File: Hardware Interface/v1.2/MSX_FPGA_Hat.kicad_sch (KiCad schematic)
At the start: 24 parts, among them J1 J1, J2 J2, J3a1 J3a, J3b1 J3b, J4a1 J4a, J4b1 J4b, U1 74LVC245A, U2 74LVC245A, U3 74LVC245A, U4 74LVC245A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

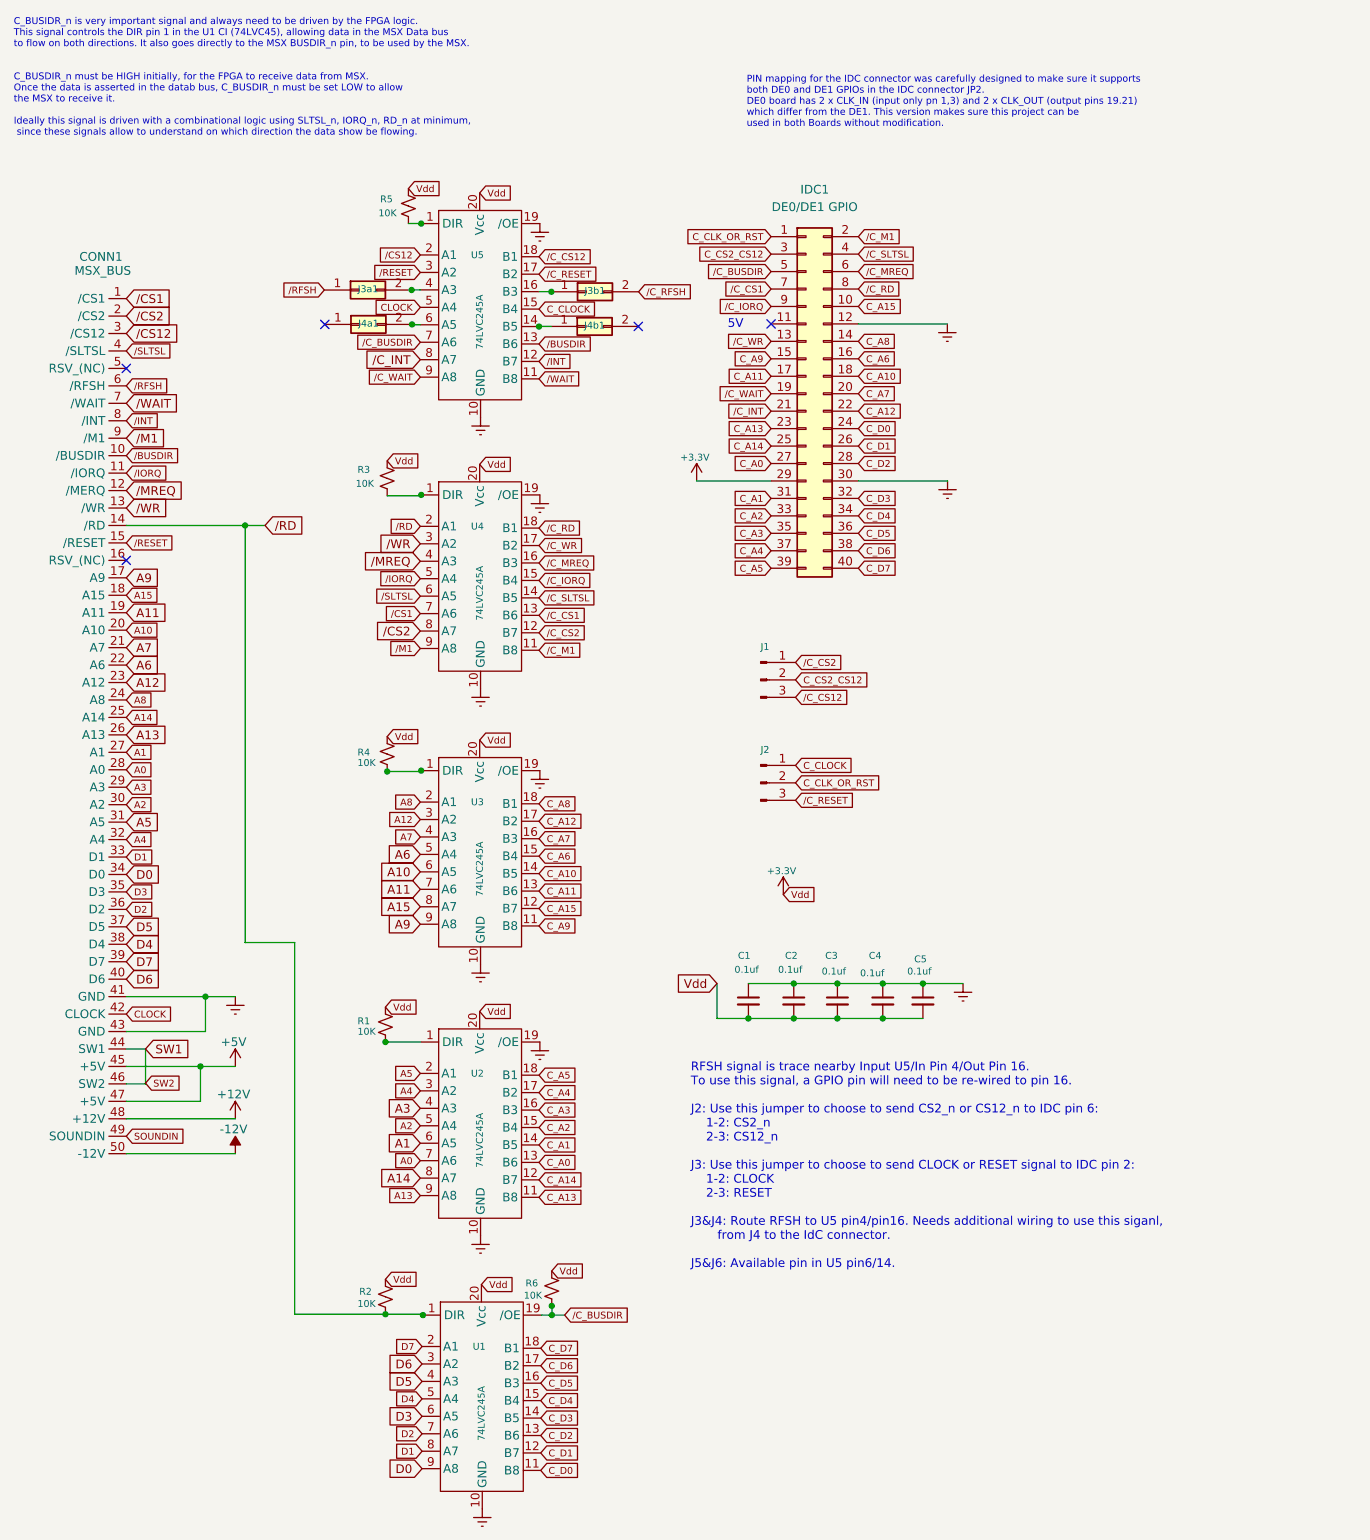
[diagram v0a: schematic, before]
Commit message: Reverted the interface schema to v1.1, as it's verified that U1 does not need to be driven by its own 7 separate pin.  BUSDIR in the FPGA will continue driving both MSX BUSDIR and U1 DIR pin
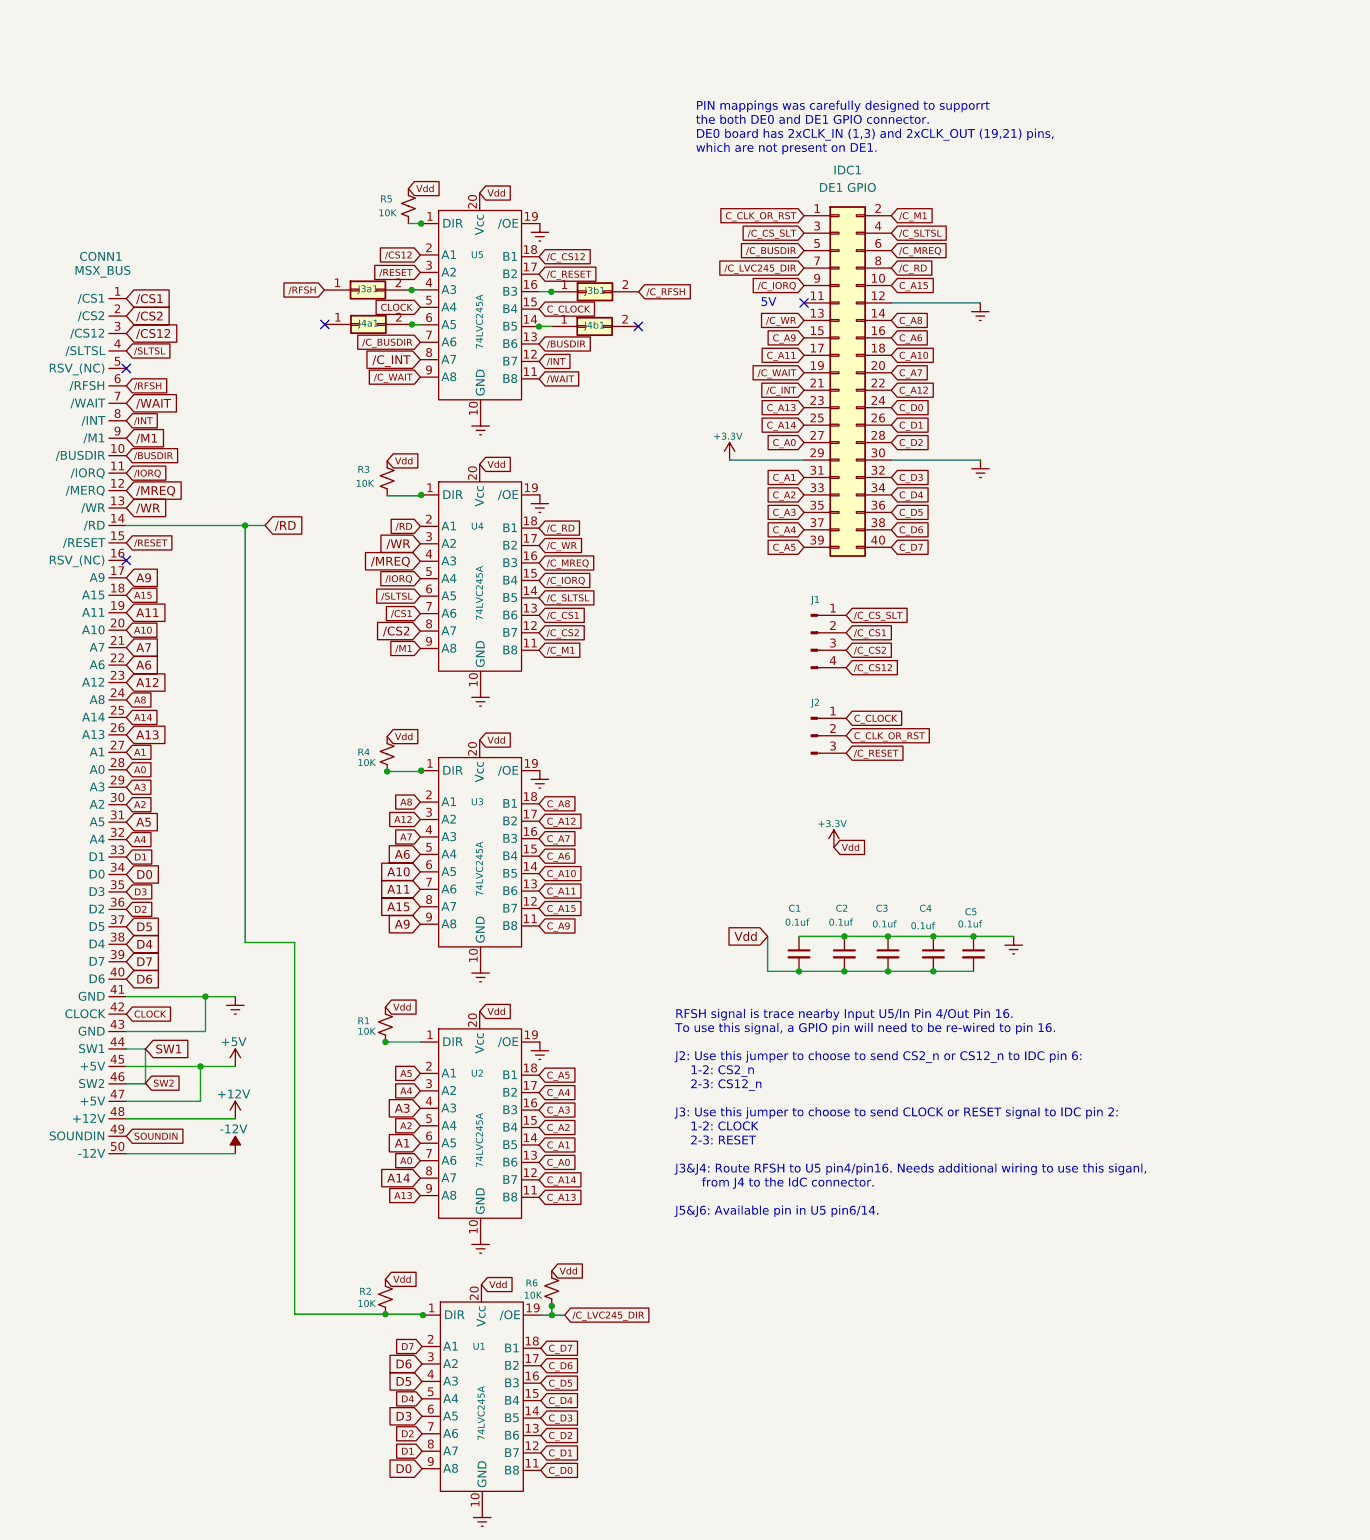
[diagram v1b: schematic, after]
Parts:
- IDC1: value DE0/DE1 GPIO -> DE1 GPIO
- J1: footprint Connector_PinHeader_2.54mm:PinHeader_1x03_P2.54mm_Vertical -> Connector_PinHeader_2.54mm:PinHeader_2x02_P2.54mm_Vertical; symbol Connector:Conn_01x03_Male -> Connector:Conn_01x04_Male
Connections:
- net /C_BUSDIR: no longer R6.2, U1.19 (/OE)
- net /C_CS1: now also J1.2 (Pin_2); no longer IDC1.7 (Pin_7)
- net /C_CS12: now also J1.4 (Pin_4); no longer J1.3 (Pin_3)
- net /C_CS2: now also J1.3 (Pin_3); no longer J1.1 (Pin_1)
- net C_CS2_CS12 renamed /C_CS_SLT
- net /C_CS_SLT: now also J1.1 (Pin_1); no longer J1.2 (Pin_2)
- new net /C_LVC245_DIR: IDC1.7 (Pin_7), R6.2, U1.19 (/OE)
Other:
- note added: "PIN mappings was carefully designed to supporrt the both DE0 and DE1 GPIO connector. DE0 board has 2xCLK_IN (1,3) and 2xCLK_OUT (19,21) pins, which are not present on DE1."
- note removed: "C_BUSIDR_n is very important signal and always need to be driven by the FPGA logic. This signal controls the DIR pin 1 in the U1 CI (74LVC45), allowing data in the MSX Data bus to flow on both directions. It also goes directly to the MSX BUSDIR_n pin, to be used by the MSX. C_BUSDIR_n must be HIGH initially, for the FPGA to receive data from MSX. Once the data is asserted in the datab bus, C_BUSD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"
- note removed: "PIN mapping for the IDC connector was carefully designed to make sure it supports both DE0 and DE1 GPIOs in the IDC connector JP2. DE0 board has 2 x CLK_IN (input only pn 1,3) and 2 x CLK_OUT (output pins 19.21) which differ from the DE1. This version makes sure this project can be used in both Boards without modification."
- moved on the sheet: C1, C2, C3, C4, C5, IDC1, J2
